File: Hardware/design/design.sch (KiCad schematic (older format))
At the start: 57 parts, among them SW1 SW_SP3T, SW10 SW_SP3T, SW11 SW_Push, SW12 SW_Push, SW13 SW_Push, SW14 SW_Push, SW15 SW_SP3T, SW16 SW_Push, SW17 SW_Push, SW18 SW_Push, SW19 SW_Push, SW2 SW_Push, SW20 SW_SP3T, SW21 SW_Push, SW22 SW_Push, SW23 SW_Push, SW24 SW_Push, SW25 SW_Push, SW26 SW_Push, SW27 SW_Push, SW28 SW_Push, SW3 SW_Push, SW4 SW_Push, SW5 SW_Push, SW6 SW_Push, SW7 SW_Push, SW8 SW_Push, SW9 SW_Push, U1 ProMicro

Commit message: added test software to make sure that library is working
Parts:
- added D1, D10, D11, D12, D2, D3, D4, D5, D6, D7, D8, D9: DIODE, symbol pspice:DIODE
- gave numbers to parts that had none: 24
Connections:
- net labels added: COL0, COL1, COL2, COL3, COL4, COL5, RAW, ROW0, ROW1, ROW2, ROW3, ROW4, ROW5, RST
- wire segments 108 -> 141
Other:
- moved on the sheet: D13, D14, D15, D16, D17, D18, D19, D20, D21, D22, D23, D24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

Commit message: chose and added 3 toggle switches
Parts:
- SW13, SW4, SW8: footprint Button_Switch_Keyboard:SW_Cherry_MX_1.00u_PCB -> digikey-footprints:Switch_Toggle_ATE1D-2M3-10-Z
- SW14, SW5, SW9: footprint Button_Switch_Keyboard:SW_Cherry_MX_1.00u_PCB -> (none)
- SW16, SW18, SW21, SW23, SW25, SW27: footprint (none) -> Button_Switch_Keyboard:SW_Cherry_MX_1.00u_PCB
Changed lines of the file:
@@
 F 0 "SW16" H 8950 965 50  0000 C CNN
 F 1 "SW_Push" H 8950 1056 50  0000 C CNN
-F 2 "" H 8950 1350 50  0001 C CNN
+F 2 "Button_Switch_Keyboard:SW_Cherry_MX_1.00u_PCB" H 8950 1350 50  0001 C CNN
 F 3 "~" H 8950 1350 50  0001 C CNN
 	1    8950 1150
@@
 F 0 "SW21" H 9600 965 50  0000 C CNN
 F 1 "SW_Push" H 9600 1056 50  0000 C CNN
-F 2 "" H 9600 1350 50  0001 C CNN
+F 2 "Button_Switch_Keyboard:SW_Cherry_MX_1.00u_PCB" H 9600 1350 50  0001 C CNN
 F 3 "~" H 9600 1350 50  0001 C CNN
 	1    9600 1150
@@
 F 0 "SW25" H 10300 965 50  0000 C CNN
 F 1 "SW_Push" H 10300 1056 50  0000 C CNN
-F 2 "" H 10300 1350 50  0001 C CNN
+F 2 "Button_Switch_Keyboard:SW_Cherry_MX_1.00u_PCB" H 10300 1350 50  0001 C CNN
 F 3 "~" H 10300 1350 50  0001 C CNN
 	1    10300 1150
@@
 F 0 "SW27" H 10350 1765 50  0000 C CNN
 F 1 "SW_Push" H 10350 1856 50  0000 C CNN
-F 2 "" H 10350 2150 50  0001 C CNN
+F 2 "Button_Switch_Keyboard:SW_Cherry_MX_1.00u_PCB" H 10350 2150 50  0001 C CNN
 F 3 "~" H 10350 2150 50  0001 C CNN
 	1    10350 1950
@@
 F 0 "SW23" H 9650 1765 50  0000 C CNN
 F 1 "SW_Push" H 9650 1856 50  0000 C CNN
-F 2 "" H 9650 2150 50  0001 C CNN
+F 2 "Button_Switch_Keyboard:SW_Cherry_MX_1.00u_PCB" H 9650 2150 50  0001 C CNN
 F 3 "~" H 9650 2150 50  0001 C CNN
 	1    9650 1950
@@
 F 0 "SW18" H 9000 1765 50  0000 C CNN
 F 1 "SW_Push" H 9000 1856 50  0000 C CNN
-F 2 "" H 9000 2150 50  0001 C CNN
+F 2 "Button_Switch_Keyboard:SW_Cherry_MX_1.00u_PCB" H 9000 2150 50  0001 C CNN
 F 3 "~" H 9000 2150 50  0001 C CNN
 	1    9000 1950
@@
 F 0 "SW4" H 6850 2665 50  0000 C CNN
 F 1 "SW_Push" H 6850 2756 50  0000 C CNN
-F 2 "Button_Switch_Keyboard:SW_Cherry_MX_1.00u_PCB" H 6850 3050 50  0001 C CNN
+F 2 "digikey-footprints:Switch_Toggle_ATE1D-2M3-10-Z" H 6850 3050 50  0001 C CNN
 F 3 "~" H 6850 3050 50  0001 C CNN
 	1    6850 2850
@@
 F 0 "SW8" H 7600 2665 50  0000 C CNN
 F 1 "SW_Push" H 7600 2756 50  0000 C CNN
-F 2 "Button_Switch_Keyboard:SW_Cherry_MX_1.00u_PCB" H 7600 3050 50  0001 C CNN
+F 2 "digikey-footprints:Switch_Toggle_ATE1D-2M3-10-Z" H 7600 3050 50  0001 C CNN
 F 3 "~" H 7600 3050 50  0001 C CNN
 	1    7600 2850
@@
 F 0 "SW13" H 8300 2665 50  0000 C CNN
 F 1 "SW_Push" H 8300 2756 50  0000 C CNN
-F 2 "Button_Switch_Keyboard:SW_Cherry_MX_1.00u_PCB" H 8300 3050 50  0001 C CNN
+F 2 "digikey-footprints:Switch_Toggle_ATE1D-2M3-10-Z" H 8300 3050 50  0001 C CNN
 F 3 "~" H 8300 3050 50  0001 C CNN
 	1    8300 2850
@@
 F 0 "SW14" H 8300 3515 50  0000 C CNN
 F 1 "SW_Push" H 8300 3606 50  0000 C CNN
-F 2 "Button_Switch_Keyboard:SW_Cherry_MX_1.00u_PCB" H 8300 3900 50  0001 C CNN
+F 2 "" H 8300 3900 50  0001 C CNN
 F 3 "~" H 8300 3900 50  0001 C CNN
 	1    8300 3700
@@
 F 0 "SW9" H 7600 3515 50  0000 C CNN
 F 1 "SW_Push" H 7600 3606 50  0000 C CNN
-F 2 "Button_Switch_Keyboard:SW_Cherry_MX_1.00u_PCB" H 7600 3900 50  0001 C CNN
+F 2 "" H 7600 3900 50  0001 C CNN
 F 3 "~" H 7600 3900 50  0001 C CNN
 	1    7600 3700
@@
 F 0 "SW5" H 6850 3515 50  0000 C CNN
 F 1 "SW_Push" H 6850 3606 50  0000 C CNN
-F 2 "Button_Switch_Keyboard:SW_Cherry_MX_1.00u_PCB" H 6850 3900 50  0001 C CNN
+F 2 "" H 6850 3900 50  0001 C CNN
 F 3 "~" H 6850 3900 50  0001 C CNN
 	1    6850 3700

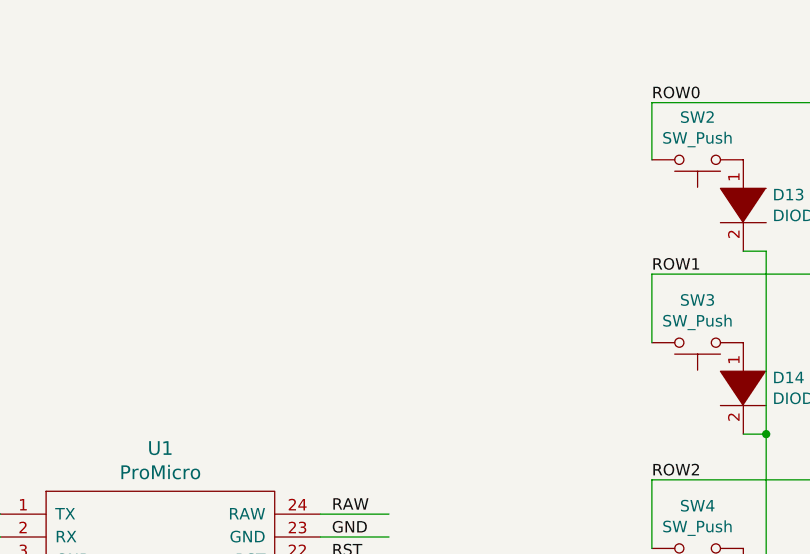
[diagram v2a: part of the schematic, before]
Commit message: added pseudocode in schematic so I won't forget scanning process
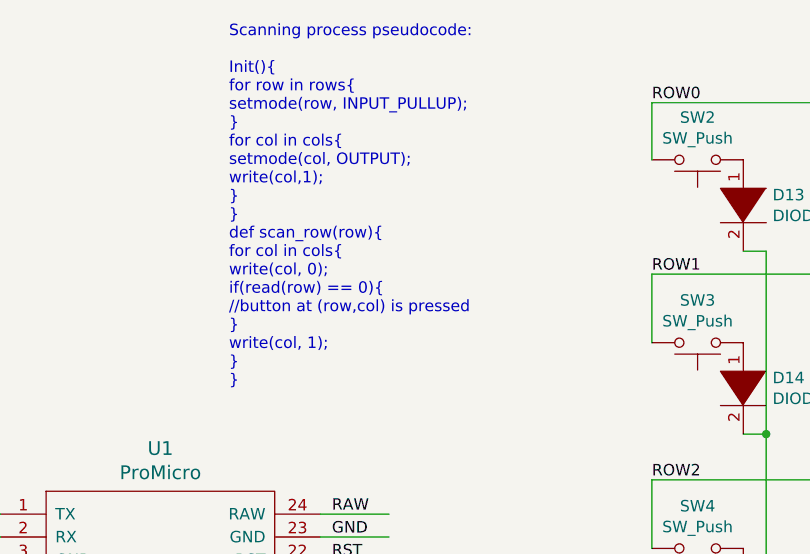
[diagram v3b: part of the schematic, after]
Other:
- note added: "Scanning process pseudocode:\n\nInit(){\nfor row in rows{\nsetmode(row, INPUT_PULLUP);\n}\nfor col in cols{\nsetmode(col, OUTPUT);\nwrite(col,1);\n} \n}\ndef scan_row(row){\nfor col in cols{\nwrite(col, 0);\nif(read(row) == 0){\n//button at (row,col) is pressed\n}\nwrite(col, 1);\n}\n}"
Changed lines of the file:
@@
 Text Label 5250 2700 0    50   ~ 0
 RAW
+Text Notes 4800 2150 0    50   ~ 0
+Scanning process pseudocode:\n\nInit(){\nfor row in rows{\nsetmode(row, INPUT_PULLUP);\n}\nfor col in cols{\nsetmode(col, OUTPUT);\nwrite(col,1);\n} \n}\ndef scan_row(row){\nfor col in cols{\nwrite(col, 0);\nif(read(row) == 0){\n//button at (row,col) is pressed\n}\nwrite(col, 1);\n}\n}
 $EndSCHEMATC

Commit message: chose rotary switches and diodes, organized layout a bit
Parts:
- removed SW1, SW10, SW15, SW20: SW_SP3T, symbol Switch:SW_SP3T
- added SW1, SW10, SW15, SW20: NKK_NR01, Kicad_Akiyuki_Footprint:NR01, symbol Akiyuki_UI:NKK_NR01
- D1, D10, D11, D12, D13, D14, D15, D16, D17, D18, D19, D2, D20, D21, D22, D23, D24, D25, D26, D27, D28, D29, D3, D30, D31, D32, D33, D34, D35, D36, D4, D5, D6, D7, D8, D9: footprint (none) -> Diode_THT:D_5KPW_P7.62mm_Vertical_AnodeUp
- SW14, SW17, SW19, SW22, SW24, SW26, SW28: footprint (none) -> Button_Switch_Keyboard:SW_Cherry_MX_1.00u_PCB
- SW5, SW9: footprint (none) -> digikey-footprints:Tilt_Switch_RB-220-07A_R
- U1: footprint Connector_PinHeader_1.00mm:PinHeader_2x12_P1.00mm_Horizontal -> promicro:ProMicro
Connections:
- net labels added: col0, col1, col2, col3, col4, col5, row4, row5
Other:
- moved on the sheet: D10, D12, D2, D4, D6, D8

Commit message: switched to 24 all cherry switches for 2 octave keyboard
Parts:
- SW13, SW4, SW8: footprint digikey-footprints:Switch_Toggle_ATE1D-2M3-10-Z -> Button_Switch_Keyboard:SW_Cherry_MX_1.00u_PCB
- SW5, SW9: footprint digikey-footprints:Tilt_Switch_RB-220-07A_R -> Button_Switch_Keyboard:SW_Cherry_MX_1.00u_PCB
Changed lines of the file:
@@
 F 0 "SW4" H 6850 2665 50  0000 C CNN
 F 1 "SW_Push" H 6850 2756 50  0000 C CNN
-F 2 "digikey-footprints:Switch_Toggle_ATE1D-2M3-10-Z" H 6850 3050 50  0001 C CNN
+F 2 "Button_Switch_Keyboard:SW_Cherry_MX_1.00u_PCB" H 6850 3050 50  0001 C CNN
 F 3 "~" H 6850 3050 50  0001 C CNN
 	1    6850 2850
@@
 F 0 "SW8" H 7600 2665 50  0000 C CNN
 F 1 "SW_Push" H 7600 2756 50  0000 C CNN
-F 2 "digikey-footprints:Switch_Toggle_ATE1D-2M3-10-Z" H 7600 3050 50  0001 C CNN
+F 2 "Button_Switch_Keyboard:SW_Cherry_MX_1.00u_PCB" H 7600 3050 50  0001 C CNN
 F 3 "~" H 7600 3050 50  0001 C CNN
 	1    7600 2850
@@
 F 0 "SW13" H 8300 2665 50  0000 C CNN
 F 1 "SW_Push" H 8300 2756 50  0000 C CNN
-F 2 "digikey-footprints:Switch_Toggle_ATE1D-2M3-10-Z" H 8300 3050 50  0001 C CNN
+F 2 "Button_Switch_Keyboard:SW_Cherry_MX_1.00u_PCB" H 8300 3050 50  0001 C CNN
 F 3 "~" H 8300 3050 50  0001 C CNN
 	1    8300 2850
@@
 F 0 "SW9" H 7600 3515 50  0000 C CNN
 F 1 "SW_Push" H 7600 3606 50  0000 C CNN
-F 2 "digikey-footprints:Tilt_Switch_RB-220-07A_R" H 7600 3900 50  0001 C CNN
+F 2 "Button_Switch_Keyboard:SW_Cherry_MX_1.00u_PCB" H 7600 3900 50  0001 C CNN
 F 3 "~" H 7600 3900 50  0001 C CNN
 	1    7600 3700
@@
 F 0 "SW5" H 6850 3515 50  0000 C CNN
 F 1 "SW_Push" H 6850 3606 50  0000 C CNN
-F 2 "digikey-footprints:Tilt_Switch_RB-220-07A_R" H 6850 3900 50  0001 C CNN
+F 2 "Button_Switch_Keyboard:SW_Cherry_MX_1.00u_PCB" H 6850 3900 50  0001 C CNN
 F 3 "~" H 6850 3900 50  0001 C CNN
 	1    6850 3700

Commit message: finished column routing, sitched to 1206 SMD diodes
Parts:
- D1, D10, D11, D12, D13, D14, D15, D16, D17, D18, D19, D2, D20, D21, D22, D23, D24, D25, D26, D27, D28, D29, D3, D30, D31, D32, D33, D34, D35, D36, D4, D5, D6, D7, D8, D9: footprint Diode_THT:D_5KPW_P7.62mm_Vertical_AnodeUp -> Diode_SMD:D_1206_3216Metric
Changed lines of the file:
@@
 F 0 "D13" V 7004 1478 50  0000 L CNN
 F 1 "DIODE" V 7095 1478 50  0000 L CNN
-F 2 "Diode_THT:D_5KPW_P7.62mm_Vertical_AnodeUp" H 7050 1350 50  0001 C CNN
+F 2 "Diode_SMD:D_1206_3216Metric" H 7050 1350 50  0001 C CNN
 F 3 "~" H 7050 1350 50  0001 C CNN
 	1    7050 1350
@@
 F 0 "D17" V 7754 1478 50  0000 L CNN
 F 1 "DIODE" V 7845 1478 50  0000 L CNN
-F 2 "Diode_THT:D_5KPW_P7.62mm_Vertical_AnodeUp" H 7800 1350 50  0001 C CNN
+F 2 "Diode_SMD:D_1206_3216Metric" H 7800 1350 50  0001 C CNN
 F 3 "~" H 7800 1350 50  0001 C CNN
 	1    7800 1350
@@
 F 0 "D21" V 8454 1478 50  0000 L CNN
 F 1 "DIODE" V 8545 1478 50  0000 L CNN
-F 2 "Diode_THT:D_5KPW_P7.62mm_Vertical_AnodeUp" H 8500 1350 50  0001 C CNN
+F 2 "Diode_SMD:D_1206_3216Metric" H 8500 1350 50  0001 C CNN
 F 3 "~" H 8500 1350 50  0001 C CNN
 	1    8500 1350
@@
 F 0 "D25" V 9104 1478 50  0000 L CNN
 F 1 "DIODE" V 9195 1478 50  0000 L CNN
-F 2 "Diode_THT:D_5KPW_P7.62mm_Vertical_AnodeUp" H 9150 1350 50  0001 C CNN
+F 2 "Diode_SMD:D_1206_3216Metric" H 9150 1350 50  0001 C CNN
 F 3 "~" H 9150 1350 50  0001 C CNN
 	1    9150 1350
@@
 F 0 "D29" V 9754 1478 50  0000 L CNN
 F 1 "DIODE" V 9845 1478 50  0000 L CNN
-F 2 "Diode_THT:D_5KPW_P7.62mm_Vertical_AnodeUp" H 9800 1350 50  0001 C CNN
+F 2 "Diode_SMD:D_1206_3216Metric" H 9800 1350 50  0001 C CNN
 F 3 "~" H 9800 1350 50  0001 C CNN
 	1    9800 1350
@@
 F 0 "D33" V 10454 1478 50  0000 L CNN
 F 1 "DIODE" V 10545 1478 50  0000 L CNN
-F 2 "Diode_THT:D_5KPW_P7.62mm_Vertical_AnodeUp" H 10500 1350 50  0001 C CNN
+F 2 "Diode_SMD:D_1206_3216Metric" H 10500 1350 50  0001 C CNN
 F 3 "~" H 10500 1350 50  0001 C CNN
 	1    10500 1350
@@
 F 0 "D34" V 10504 2278 50  0000 L CNN
 F 1 "DIODE" V 10595 2278 50  0000 L CNN
-F 2 "Diode_THT:D_5KPW_P7.62mm_Vertical_AnodeUp" H 10550 2150 50  0001 C CNN
+F 2 "Diode_SMD:D_1206_3216Metric" H 10550 2150 50  0001 C CNN
 F 3 "~" H 10550 2150 50  0001 C CNN
 	1    10550 2150
@@
 F 0 "D30" V 9804 2278 50  0000 L CNN
 F 1 "DIODE" V 9895 2278 50  0000 L CNN
-F 2 "Diode_THT:D_5KPW_P7.62mm_Vertical_AnodeUp" H 9850 2150 50  0001 C CNN
+F 2 "Diode_SMD:D_1206_3216Metric" H 9850 2150 50  0001 C CNN
 F 3 "~" H 9850 2150 50  0001 C CNN
 	1    9850 2150
@@
 F 0 "D26" V 9154 2278 50  0000 L CNN
 F 1 "DIODE" V 9245 2278 50  0000 L CNN
-F 2 "Diode_THT:D_5KPW_P7.62mm_Vertical_AnodeUp" H 9200 2150 50  0001 C CNN
+F 2 "Diode_SMD:D_1206_3216Metric" H 9200 2150 50  0001 C CNN
 F 3 "~" H 9200 2150 50  0001 C CNN
 	1    9200 2150
@@
 F 0 "D22" V 8454 2278 50  0000 L CNN
 F 1 "DIODE" V 8545 2278 50  0000 L CNN
-F 2 "Diode_THT:D_5KPW_P7.62mm_Vertical_AnodeUp" H 8500 2150 50  0001 C CNN
+F 2 "Diode_SMD:D_1206_3216Metric" H 8500 2150 50  0001 C CNN
 F 3 "~" H 8500 2150 50  0001 C CNN
 	1    8500 2150
@@
 F 0 "D18" V 7754 2278 50  0000 L CNN
 F 1 "DIODE" V 7845 2278 50  0000 L CNN
-F 2 "Diode_THT:D_5KPW_P7.62mm_Vertical_AnodeUp" H 7800 2150 50  0001 C CNN
+F 2 "Diode_SMD:D_1206_3216Metric" H 7800 2150 50  0001 C CNN
 F 3 "~" H 7800 2150 50  0001 C CNN
 	1    7800 2150
@@
 F 0 "D14" V 7004 2278 50  0000 L CNN
 F 1 "DIODE" V 7095 2278 50  0000 L CNN
-F 2 "Diode_THT:D_5KPW_P7.62mm_Vertical_AnodeUp" H 7050 2150 50  0001 C CNN
+F 2 "Diode_SMD:D_1206_3216Metric" H 7050 2150 50  0001 C CNN
 F 3 "~" H 7050 2150 50  0001 C CNN
 	1    7050 2150
@@
 F 0 "D15" V 7004 3178 50  0000 L CNN
 F 1 "DIODE" V 7095 3178 50  0000 L CNN
-F 2 "Diode_THT:D_5KPW_P7.62mm_Vertical_AnodeUp" H 7050 3050 50  0001 C CNN
+F 2 "Diode_SMD:D_1206_3216Metric" H 7050 3050 50  0001 C CNN
 F 3 "~" H 7050 3050 50  0001 C CNN
 	1    7050 3050
@@
 F 0 "D19" V 7754 3178 50  0000 L CNN
 F 1 "DIODE" V 7845 3178 50  0000 L CNN
-F 2 "Diode_THT:D_5KPW_P7.62mm_Vertical_AnodeUp" H 7800 3050 50  0001 C CNN
+F 2 "Diode_SMD:D_1206_3216Metric" H 7800 3050 50  0001 C CNN
 F 3 "~" H 7800 3050 50  0001 C CNN
 	1    7800 3050
@@
 F 0 "D23" V 8454 3178 50  0000 L CNN
 F 1 "DIODE" V 8545 3178 50  0000 L CNN
-F 2 "Diode_THT:D_5KPW_P7.62mm_Vertical_AnodeUp" H 8500 3050 50  0001 C CNN
+F 2 "Diode_SMD:D_1206_3216Metric" H 8500 3050 50  0001 C CNN
 F 3 "~" H 8500 3050 50  0001 C CNN
 	1    8500 3050
@@
 F 0 "D27" V 9154 3178 50  0000 L CNN
 F 1 "DIODE" V 9245 3178 50  0000 L CNN
-F 2 "Diode_THT:D_5KPW_P7.62mm_Vertical_AnodeUp" H 9200 3050 50  0001 C CNN
+F 2 "Diode_SMD:D_1206_3216Metric" H 9200 3050 50  0001 C CNN
 F 3 "~" H 9200 3050 50  0001 C CNN
 	1    9200 3050
@@
 F 0 "D31" V 9804 3178 50  0000 L CNN
 F 1 "DIODE" V 9895 3178 50  0000 L CNN
-F 2 "Diode_THT:D_5KPW_P7.62mm_Vertical_AnodeUp" H 9850 3050 50  0001 C CNN
+F 2 "Diode_SMD:D_1206_3216Metric" H 9850 3050 50  0001 C CNN
 F 3 "~" H 9850 3050 50  0001 C CNN
 	1    9850 3050
@@
 F 0 "D35" V 10504 3178 50  0000 L CNN
 F 1 "DIODE" V 10595 3178 50  0000 L CNN
-F 2 "Diode_THT:D_5KPW_P7.62mm_Vertical_AnodeUp" H 10550 3050 50  0001 C CNN
+F 2 "Diode_SMD:D_1206_3216Metric" H 10550 3050 50  0001 C CNN
 F 3 "~" H 10550 3050 50  0001 C CNN
 	1    10550 3050
@@
 F 0 "D36" V 10504 4028 50  0000 L CNN
 F 1 "DIODE" V 10595 4028 50  0000 L CNN
-F 2 "Diode_THT:D_5KPW_P7.62mm_Vertical_AnodeUp" H 10550 3900 50  0001 C CNN
+F 2 "Diode_SMD:D_1206_3216Metric" H 10550 3900 50  0001 C CNN
 F 3 "~" H 10550 3900 50  0001 C CNN
 	1    10550 3900
@@
 F 0 "D32" V 9804 4028 50  0000 L CNN
 F 1 "DIODE" V 9895 4028 50  0000 L CNN
-F 2 "Diode_THT:D_5KPW_P7.62mm_Vertical_AnodeUp" H 9850 3900 50  0001 C CNN
+F 2 "Diode_SMD:D_1206_3216Metric" H 9850 3900 50  0001 C CNN
 F 3 "~" H 9850 3900 50  0001 C CNN
 	1    9850 3900
@@
 F 0 "D28" V 9154 4028 50  0000 L CNN
 F 1 "DIODE" V 9245 4028 50  0000 L CNN
-F 2 "Diode_THT:D_5KPW_P7.62mm_Vertical_AnodeUp" H 9200 3900 50  0001 C CNN
+F 2 "Diode_SMD:D_1206_3216Metric" H 9200 3900 50  0001 C CNN
 F 3 "~" H 9200 3900 50  0001 C CNN
 	1    9200 3900
@@
 F 0 "D24" V 8454 4028 50  0000 L CNN
 F 1 "DIODE" V 8545 4028 50  0000 L CNN
-F 2 "Diode_THT:D_5KPW_P7.62mm_Vertical_AnodeUp" H 8500 3900 50  0001 C CNN
+F 2 "Diode_SMD:D_1206_3216Metric" H 8500 3900 50  0001 C CNN
 F 3 "~" H 8500 3900 50  0001 C CNN
 	1    8500 3900
@@
 F 0 "D20" V 7754 4028 50  0000 L CNN
 F 1 "DIODE" V 7845 4028 50  0000 L CNN
-F 2 "Diode_THT:D_5KPW_P7.62mm_Vertical_AnodeUp" H 7800 3900 50  0001 C CNN
+F 2 "Diode_SMD:D_1206_3216Metric" H 7800 3900 50  0001 C CNN
 F 3 "~" H 7800 3900 50  0001 C CNN
 	1    7800 3900
@@
 F 0 "D16" V 7004 4028 50  0000 L CNN
 F 1 "DIODE" V 7095 4028 50  0000 L CNN
-F 2 "Diode_THT:D_5KPW_P7.62mm_Vertical_AnodeUp" H 7050 3900 50  0001 C CNN
+F 2 "Diode_SMD:D_1206_3216Metric" H 7050 3900 50  0001 C CNN
 F 3 "~" H 7050 3900 50  0001 C CNN
 	1    7050 3900
@@
 F 0 "D4" V 1754 6878 50  0000 L CNN
 F 1 "DIODE" V 1845 6878 50  0000 L CNN
-F 2 "Diode_THT:D_5KPW_P7.62mm_Vertical_AnodeUp" H 1800 6750 50  0001 C CNN
+F 2 "Diode_SMD:D_1206_3216Metric" H 1800 6750 50  0001 C CNN
 F 3 "~" H 1800 6750 50  0001 C CNN
 	1    1800 6750
@@
 F 0 "D2" V 1254 6878 50  0000 L CNN
 F 1 "DIODE" V 1345 6878 50  0000 L CNN
-F 2 "Diode_THT:D_5KPW_P7.62mm_Vertical_AnodeUp" H 1300 6750 50  0001 C CNN
+F 2 "Diode_SMD:D_1206_3216Metric" H 1300 6750 50  0001 C CNN
 F 3 "~" H 1300 6750 50  0001 C CNN
 	1    1300 6750
@@
 F 0 "D6" V 2454 6878 50  0000 L CNN
 F 1 "DIODE" V 2545 6878 50  0000 L CNN
-F 2 "Diode_THT:D_5KPW_P7.62mm_Vertical_AnodeUp" H 2500 6750 50  0001 C CNN
+F 2 "Diode_SMD:D_1206_3216Metric" H 2500 6750 50  0001 C CNN
 F 3 "~" H 2500 6750 50  0001 C CNN
 	1    2500 6750
@@
 F 0 "D12" V 3854 6878 50  0000 L CNN
 F 1 "DIODE" V 3945 6878 50  0000 L CNN
-F 2 "Diode_THT:D_5KPW_P7.62mm_Vertical_AnodeUp" H 3900 6750 50  0001 C CNN
+F 2 "Diode_SMD:D_1206_3216Metric" H 3900 6750 50  0001 C CNN
 F 3 "~" H 3900 6750 50  0001 C CNN
 	1    3900 6750
@@
 F 0 "D8" V 5054 6878 50  0000 L CNN
 F 1 "DIODE" V 5145 6878 50  0000 L CNN
-F 2 "Diode_THT:D_5KPW_P7.62mm_Vertical_AnodeUp" H 5100 6750 50  0001 C CNN
+F 2 "Diode_SMD:D_1206_3216Metric" H 5100 6750 50  0001 C CNN
 F 3 "~" H 5100 6750 50  0001 C CNN
 	1    5100 6750
@@
 F 0 "D10" V 4554 6878 50  0000 L CNN
 F 1 "DIODE" V 4645 6878 50  0000 L CNN
-F 2 "Diode_THT:D_5KPW_P7.62mm_Vertical_AnodeUp" H 4600 6750 50  0001 C CNN
+F 2 "Diode_SMD:D_1206_3216Metric" H 4600 6750 50  0001 C CNN
 F 3 "~" H 4600 6750 50  0001 C CNN
 	1    4600 6750
@@
 F 0 "D3" V 1754 5778 50  0000 L CNN
 F 1 "DIODE" V 1845 5778 50  0000 L CNN
-F 2 "Diode_THT:D_5KPW_P7.62mm_Vertical_AnodeUp" H 1800 5650 50  0001 C CNN
+F 2 "Diode_SMD:D_1206_3216Metric" H 1800 5650 50  0001 C CNN
 F 3 "~" H 1800 5650 50  0001 C CNN
 	1    1800 5650
@@
 F 0 "D1" V 1254 5778 50  0000 L CNN
 F 1 "DIODE" V 1345 5778 50  0000 L CNN
-F 2 "Diode_THT:D_5KPW_P7.62mm_Vertical_AnodeUp" H 1300 5650 50  0001 C CNN
+F 2 "Diode_SMD:D_1206_3216Metric" H 1300 5650 50  0001 C CNN
 F 3 "~" H 1300 5650 50  0001 C CNN
 	1    1300 5650
@@
 F 0 "D5" V 2454 5778 50  0000 L CNN
 F 1 "DIODE" V 2545 5778 50  0000 L CNN
-F 2 "Diode_THT:D_5KPW_P7.62mm_Vertical_AnodeUp" H 2500 5650 50  0001 C CNN
+F 2 "Diode_SMD:D_1206_3216Metric" H 2500 5650 50  0001 C CNN
 F 3 "~" H 2500 5650 50  0001 C CNN
 	1    2500 5650
@@
 F 0 "D7" V 3854 5778 50  0000 L CNN
 F 1 "DIODE" V 3945 5778 50  0000 L CNN
-F 2 "Diode_THT:D_5KPW_P7.62mm_Vertical_AnodeUp" H 3900 5650 50  0001 C CNN
+F 2 "Diode_SMD:D_1206_3216Metric" H 3900 5650 50  0001 C CNN
 F 3 "~" H 3900 5650 50  0001 C CNN
 	1    3900 5650
@@
 F 0 "D11" V 5054 5778 50  0000 L CNN
 F 1 "DIODE" V 5145 5778 50  0000 L CNN
-F 2 "Diode_THT:D_5KPW_P7.62mm_Vertical_AnodeUp" H 5100 5650 50  0001 C CNN
+F 2 "Diode_SMD:D_1206_3216Metric" H 5100 5650 50  0001 C CNN
 F 3 "~" H 5100 5650 50  0001 C CNN
 	1    5100 5650
@@
 F 0 "D9" V 4554 5778 50  0000 L CNN
 F 1 "DIODE" V 4645 5778 50  0000 L CNN
-F 2 "Diode_THT:D_5KPW_P7.62mm_Vertical_AnodeUp" H 4600 5650 50  0001 C CNN
+F 2 "Diode_SMD:D_1206_3216Metric" H 4600 5650 50  0001 C CNN
 F 3 "~" H 4600 5650 50  0001 C CNN
 	1    4600 5650
